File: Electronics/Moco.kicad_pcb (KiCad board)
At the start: 2 copper layers, 34 x 34 mm, 36 parts, among them J1 Conn_01x04, J2 Conn_01x01, J3 Conn_ARM_JTAG_SWD_10, J4 Conn_01x03, J5 Conn_01x01, J6 Conn_01x04, J8 Conn_01x01, J9 Conn_01x01, U1 EFM32PG22C200FxxIM32, U2 SP485EN, U3 TMAG5273, U4 DRV8311, Y1 ECS-384-CDX-1983

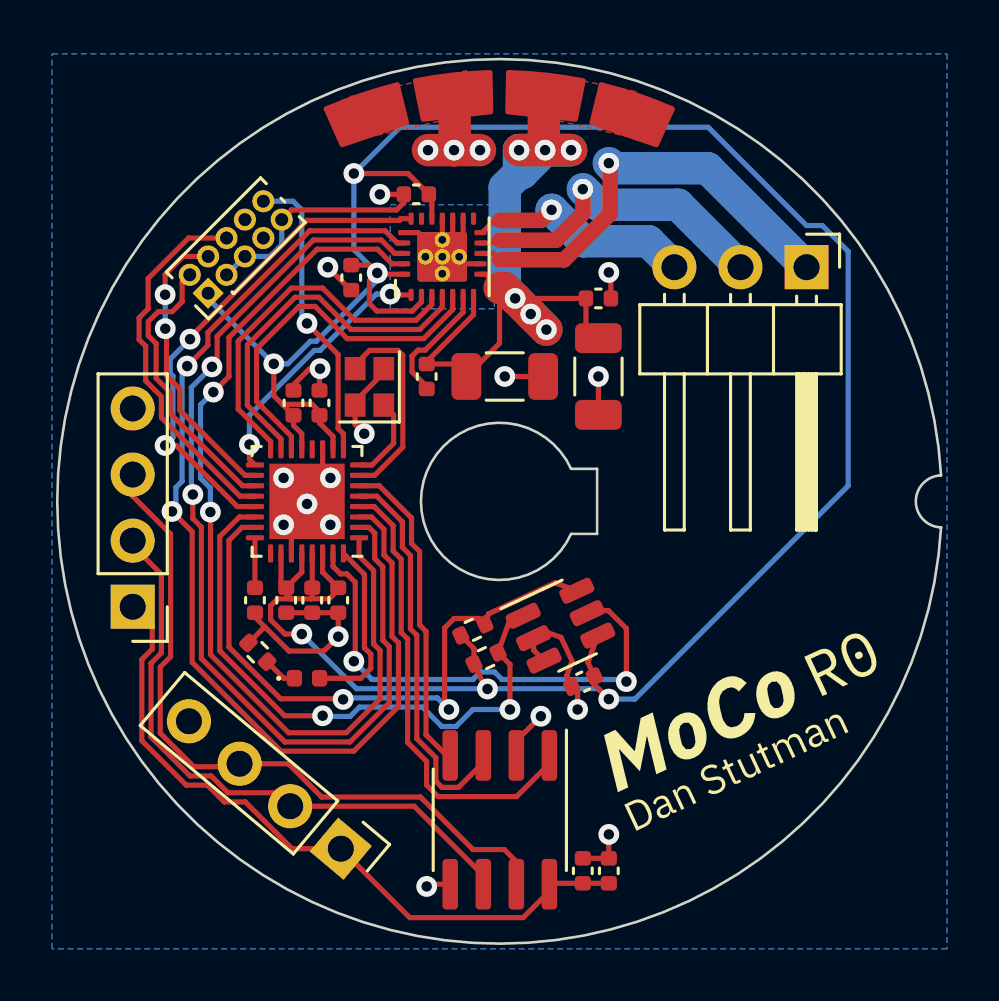
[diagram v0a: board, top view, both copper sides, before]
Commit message: Trade nFAULT for nSCS to avoid power on indeterminacy
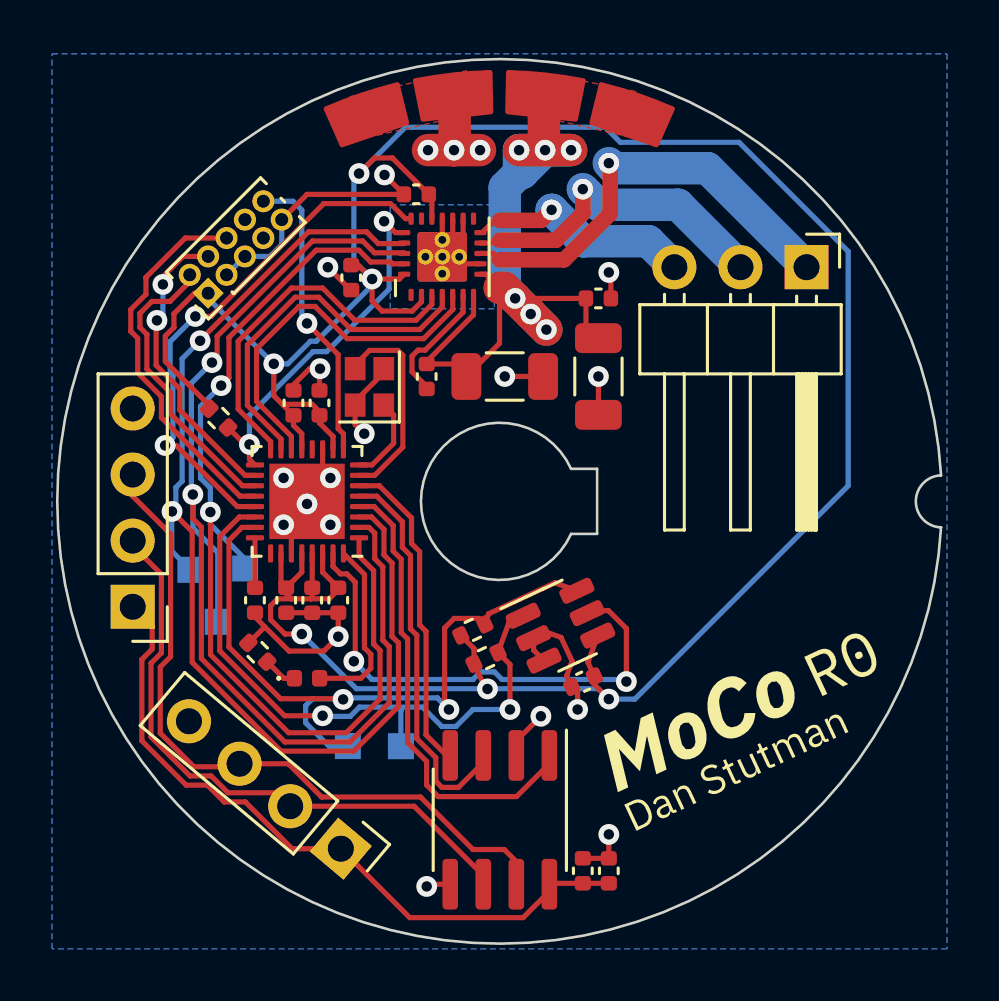
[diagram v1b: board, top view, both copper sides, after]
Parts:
- added R4: 10 kR, Resistor_SMD:R_0402_1005Metric, F.Cu at (39.2, 46.8)
- added TP1: TestPoint, TestPoint:TestPoint_Pad_1.0x1.0mm, B.Cu at (46.2, 59.4)
- added TP2: TestPoint, TestPoint:TestPoint_Pad_1.0x1.0mm, B.Cu at (40.2, 52.6)
- added TP3: TestPoint, TestPoint:TestPoint_Pad_1.0x1.0mm, B.Cu at (44.2, 59.4)
- added TP4: TestPoint, TestPoint:TestPoint_Pad_1.0x1.0mm, B.Cu at (39.2, 54.6)
- added TP5: TestPoint, TestPoint:TestPoint_Pad_1.0x1.0mm, B.Cu at (38.1, 52.6)
- added kibuzzard-624C45BD: G***, kibuzzard-624C45BD, B.Cu at (38.0, 51.2)
- added kibuzzard-624C45C7: G***, kibuzzard-624C45C7, B.Cu at (40.2, 51.2)
- added kibuzzard-624C45D0: G***, kibuzzard-624C45D0, B.Cu at (39.2, 56.0)
- added kibuzzard-624C45D8: G***, kibuzzard-624C45D8, B.Cu at (46.2, 60.8)
- added kibuzzard-624C45E2: G***, kibuzzard-624C45E2, B.Cu at (44.2, 60.8)
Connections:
- U1 pad 17: /~{FAULT} -> /DRV_~{SCS}
- U4 pad 1: /~{FAULT} -> unconnected-(U4-Pad1)
- U4 pad 20: GND -> /DRV_~{SCS}
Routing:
- net /DRV_~{SCS}: track 0.00 -> 14.1 mm, vias 0 -> 2
- net /~{FAULT}: track 10.2 -> 0.00 mm, vias 2 -> 0
- net +3V3: track 103.2 -> 108.9 mm
- net /SDI: track 38.5 -> 43.8 mm
- net /TMS_SCL: track 23.9 -> 28.2 mm
- net /SCLK: track 36.0 -> 38.7 mm
- net /SDO: track 41.2 -> 43.7 mm
- net GND: track 49.7 -> 47.7 mm
- net /TMS_SDA: track 23.2 -> 24.7 mm
- net /PWM_SYNC: track 19.5 -> 20.3 mm

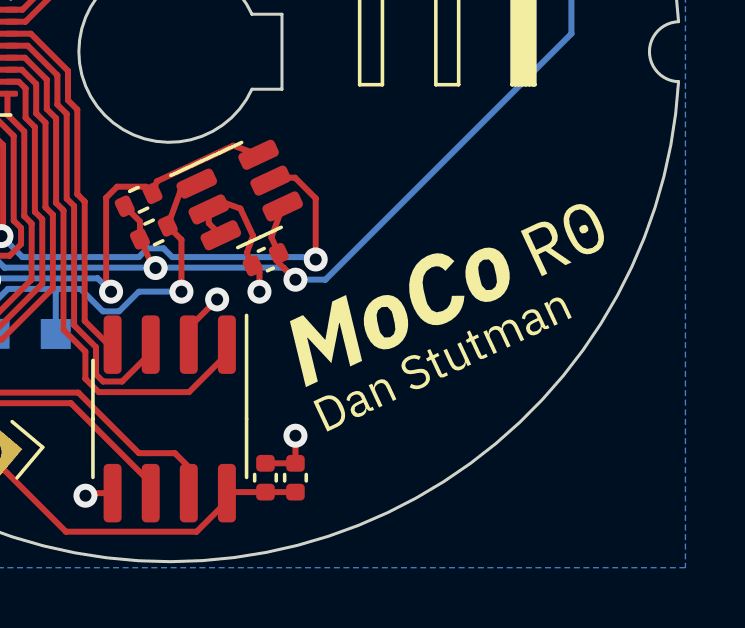
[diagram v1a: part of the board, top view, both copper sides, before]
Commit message: Update versioning scheme
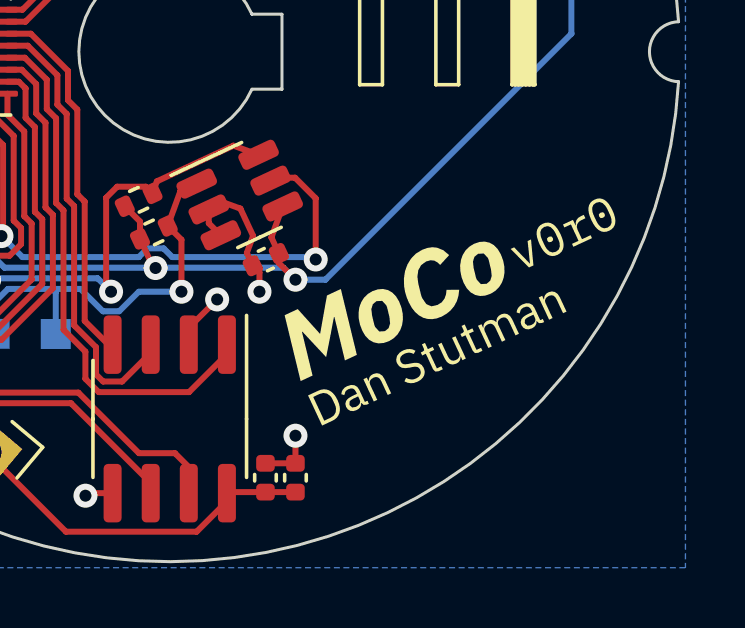
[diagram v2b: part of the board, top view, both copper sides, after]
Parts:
- removed kibuzzard-6246204B: G***, kibuzzard-6246204B
- added kibuzzard-624C491C: G***, kibuzzard-624C491C, F.Cu at (63.1, 56.0)
- moved kibuzzard-6244D452 0.27 mm to (58.9, 60.1)
- moved kibuzzard-6244CA09 0.27 mm to (57.5, 58.3)

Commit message: Update silk (I think)
I am not entirely sure what changes are in this commit. I think it is mostly
just silk modifications.
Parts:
- added kibuzzard-6257E5BB: G***, kibuzzard-6257E5BB, F.Cu at (38.2, 52.0)
- added kibuzzard-6257E5C8: G***, kibuzzard-6257E5C8, F.Cu at (44.0, 60.0)
- added kibuzzard-6257E666: G***, kibuzzard-6257E666, F.Cu at (34.0, 50.2)
- added kibuzzard-6257E666: G***, kibuzzard-6257E666, F.Cu at (39.8, 62.5)
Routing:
- net Vdrive: track 31.7 -> 32.7 mm
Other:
- outline, holes or cut-outs redrawn

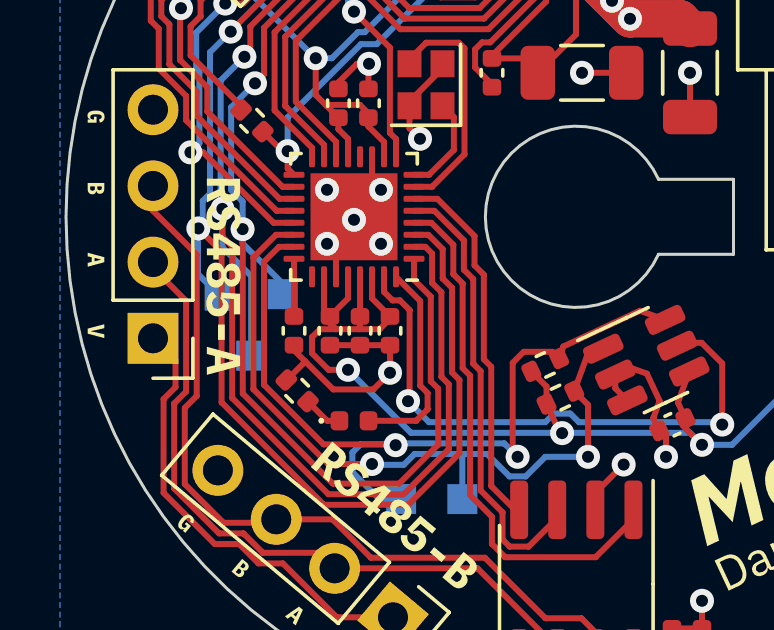
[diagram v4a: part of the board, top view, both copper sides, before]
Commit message: Update EFR32 part number
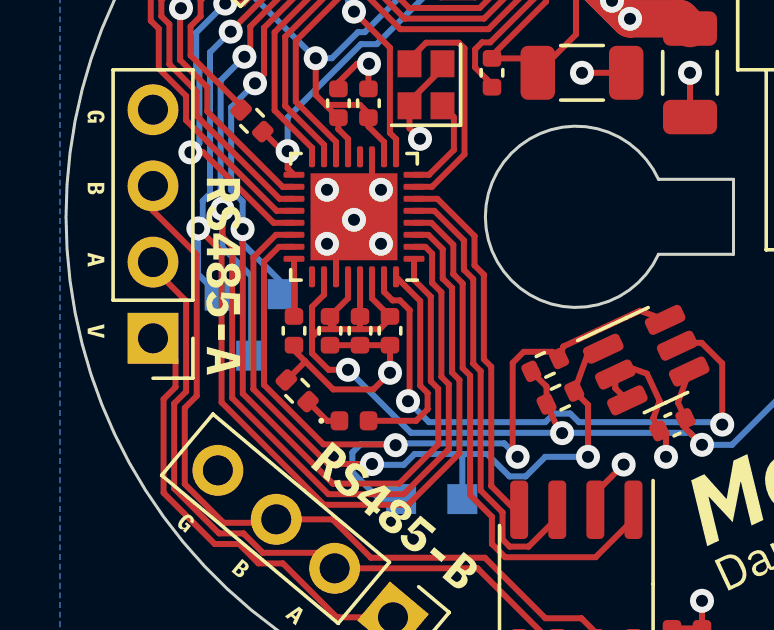
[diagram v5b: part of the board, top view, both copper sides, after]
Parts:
- C16: value 1 uF 6.3V X5R -> 0.1 uF 6.3V X5R
- C4: value 0.1 uF 6.3V X5R -> 1 uF 6.3V X5R
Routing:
- net +3V3: track 108.9 -> 110.3 mm
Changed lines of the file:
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@@
   (net 30 "/SWDIO")
   (net 31 "/SWCLK")
-  (net 32 "Net-(Y1-Pad3)")
-  (net 33 "Net-(Y1-Pad1)")
+  (net 32 "Net-(U1-Pad7)")
+  (net 33 "Net-(U1-Pad8)")
   (net 34 "unconnected-(J3-Pad7)")
   (net 35 "+5V")
@@
       (effects (font (size 1 1) (thickness 0.15)))
     )
-    (fp_text value "1 uF 6.3V X5R" (at 0 1.16 90) (layer "F.Fab") hide
+    (fp_text value "0.1 uF 6.3V X5R" (at 0 1.16 90) (layer "F.Fab") hide
       (effects (font (size 1 1) (thickness 0.15)))
     )
@@
       (net 5 "/UART_TX") (pinfunction "PC05") (pintype "bidirectional"))
     (pad "7" smd roundrect (at -2 1 180) (size 0.7 0.2) (layers "F.Cu" "F.Paste" "F.Mask") (roundrect_rratio 0.25)
-      (net 32 "Net-(Y1-Pad3)") (pinfunction "HFXTAL_I") (pintype "input"))
+      (net 32 "Net-(U1-Pad7)") (pinfunction "HFXTAL_I") (pintype "input"))
     (pad "8" smd roundrect (at -2 1.4 180) (size 0.7 0.2) (layers "F.Cu" "F.Paste" "F.Mask") (roundrect_rratio 0.25)
-      (net 33 "Net-(Y1-Pad1)") (pinfunction "HFXTAL_O") (pintype "output"))
+      (net 33 "Net-(U1-Pad8)") (pinfunction "HFXTAL_O") (pintype "output"))
     (pad "9" smd roundrect (at -1.4 2 180) (size 0.2 0.7) (layers "F.Cu" "F.Paste" "F.Mask") (roundrect_rratio 0.25)
       (net 10 "/~{RESET}") (pinfunction "~{RESET}") (pintype "input"))
@@
     (fp_line (start -1 0.3) (end -0.5 0.8) (layer "F.Fab") (width 0.1))
     (pad "1" smd rect (at -0.7 0.55 90) (size 0.9 0.8) (layers "F.Cu" "F.Paste" "F.Mask")
-      (net 33 "Net-(Y1-Pad1)") (pinfunction "1") (pintype "passive"))
+      (net 33 "Net-(U1-Pad8)") (pinfunction "1") (pintype "passive"))
     (pad "2" smd rect (at 0.7 0.55 90) (size 0.9 0.8) (layers "F.Cu" "F.Paste" "F.Mask")
       (net 2 "GND") (pinfunction "2") (pintype "passive"))
     (pad "3" smd rect (at 0.7 -0.55 90) (size 0.9 0.8) (layers "F.Cu" "F.Paste" "F.Mask")
-      (net 32 "Net-(Y1-Pad3)") (pinfunction "3") (pintype "passive"))
+      (net 32 "Net-(U1-Pad7)") (pinfunction "3") (pintype "passive"))
     (pad "4" smd rect (at -0.7 -0.55 90) (size 0.9 0.8) (layers "F.Cu" "F.Paste" "F.Mask")
       (net 2 "GND") (pinfunction "4") (pintype "passive"))
@@
       (effects (font (size 1 1) (thickness 0.15)))
     )
-    (fp_text value "0.1 uF 6.3V X5R" (at 0 1.16 90) (layer "F.Fab") hide
+    (fp_text value "1 uF 6.3V X5R" (at 0 1.16 90) (layer "F.Fab") hide
       (effects (font (size 1 1) (thickness 0.15)))
     )
@@
     (effects (font (size 0.5 0.5) (thickness 0.125)))
   )
-  (segment (start 41.6 52) (end 41.6 53.12) (width 0.2) (layer "F.Cu") (net 1))
   (segment (start 42 53.74648) (end 42.74648 53.74648) (width 0.2) (layer "F.Cu") (net 1))
   (segment (start 45.101554 42.301554) (end 45.485921 42.685921) (width 0.2) (layer "F.Cu") (net 1))
   (segment (start 41.8 53.32) (end 41.8 53.54648) (width 0.2) (layer "F.Cu") (net 1))
   (segment (start 38.275795 42) (end 38.8 42) (width 0.2) (layer "F.Cu") (net 1))
-  (segment (start 41.6 53.12) (end 41.8 53.32) (width 0.2) (layer "F.Cu") (net 1))
   (segment (start 42.4 52) (end 42.4 52.72) (width 0.2) (layer "F.Cu") (net 1))
   (segment (start 43.8 53.4) (end 43.45352 53.74648) (width 0.2) (layer "F.Cu") (net 1))
+  (segment (start 41.6 52) (end 41.6 52.6) (width 0.2) (layer "F.Cu") (net 1))
+  (segment (start 41.2 54.01348) (end 41.467 53.74648) (width 0.2) (layer "F.Cu") (net 1))
   (segment (start 45.485921 42.685921) (end 46.643321 42.685921) (width 0.2) (layer "F.Cu") (net 1))
   (segment (start 38.839376 46.308919) (end 37.15352 44.623063) (width 0.2) (layer "F.Cu") (net 1))
   (segment (start 47 42.329242) (end 47 42.065) (width 0.2) (layer "F.Cu") (net 1))
-  (segment (start 41.2 54.546521) (end 41.2 54.013479) (width 0.2) (layer "F.Cu") (net 1))
   (segment (start 45.101554 41.4535) (end 46.1515 41.4535) (width 0.2) (layer "F.Cu") (net 1))
   (segment (start 42.8 46.269192) (end 43.08 46.549192) (width 0.2) (layer "F.Cu") (net 1))
@@
   (segment (start 42.4 48) (end 42.4 47.4) (width 0.2) (layer "F.Cu") (net 1))
   (segment (start 49.017402 56.239137) (end 49.456925 57.181697) (width 0.2) (layer "F.Cu") (net 1))
-  (segment (start 41.2 54.013479) (end 41.466999 53.74648) (width 0.2) (layer "F.Cu") (net 1))
   (segment (start 42.4 47.4) (end 42.08 47.08) (width 0.2) (layer "F.Cu") (net 1))
   (segment (start 46.643321 42.685921) (end 47 42.329242) (width 0.2) (layer "F.Cu") (net 1))
   (segment (start 45.88 36.8) (end 47.28 38.2) (width 0.2) (layer "F.Cu") (net 1))
+  (segment (start 41.6 52.6) (end 41.2 53) (width 0.2) (layer "F.Cu") (net 1))
   (segment (start 37.15352 44.623063) (end 37.15352 43.648395) (width 0.2) (layer "F.Cu") (net 1))
   (segment (start 42.8 53.69296) (end 42.74648 53.74648) (width 0.2) (layer "F.Cu") (net 1))
   (segment (start 42.8 52) (end 42.8 53.32) (width 0.2) (layer "F.Cu") (net 1))
-  (segment (start 41.466999 53.74648) (end 42 53.74648) (width 0.2) (layer "F.Cu") (net 1))
+  (segment (start 41.2 54.546521) (end 41.2 54.01348) (width 0.2) (layer "F.Cu") (net 1))
   (segment (start 42.4 52.72) (end 41.8 53.32) (width 0.2) (layer "F.Cu") (net 1))
   (segment (start 54.2 57.6) (end 53.647854 57.047854) (width 0.2) (layer "F.Cu") (net 1))
   (segment (start 43.2 52.72) (end 43.8 53.32) (width 0.2) (layer "F.Cu") (net 1))
+  (segment (start 41.2 53) (end 41.2 54.546521) (width 0.2) (layer "F.Cu") (net 1))
   (segment (start 45.101554 41.4535) (end 45.101554 42.301554) (width 0.2) (layer "F.Cu") (net 1))
   (segment (start 45.101554 41.4535) (end 44.568054 40.92) (width 0.2) (layer "F.Cu") (net 1))
@@
   (segment (start 37.15352 43.648395) (end 37.485952 43.315963) (width 0.2) (layer "F.Cu") (net 1))
   (segment (start 43.6 47.506974) (end 43.08 46.986974) (width 0.2) (layer "F.Cu") (net 1))
+  (segment (start 41.467 53.74648) (end 42 53.74648) (width 0.2) (layer "F.Cu") (net 1))
   (via (at 44.6 37.4) (size 0.8) (drill 0.4) (layers "F.Cu" "B.Cu") (net 1))
   (via (at 42.4 55.100011) (size 0.8) (drill 0.4) (layers "F.Cu" "B.Cu") (net 1))
@@
   (group "" (id 093e0f3c-a4b3-4709-98e0-957c66f7e9e6)
     (members
-      03015993-67fa-4265-87b3-b7c734d16a0b
       0d3ee6ec-df59-456d-90a9-116ce4aef184
       1382190d-a40b-40df-b429-059cb272fba8
-      1f171868-fac2-4e0d-9075-5f6cd6da7010
       24baab14-c1ed-4f83-868b-cbafc0523fee
       2b6dc378-9ac7-4bdd-b185-57e1888b7bfc

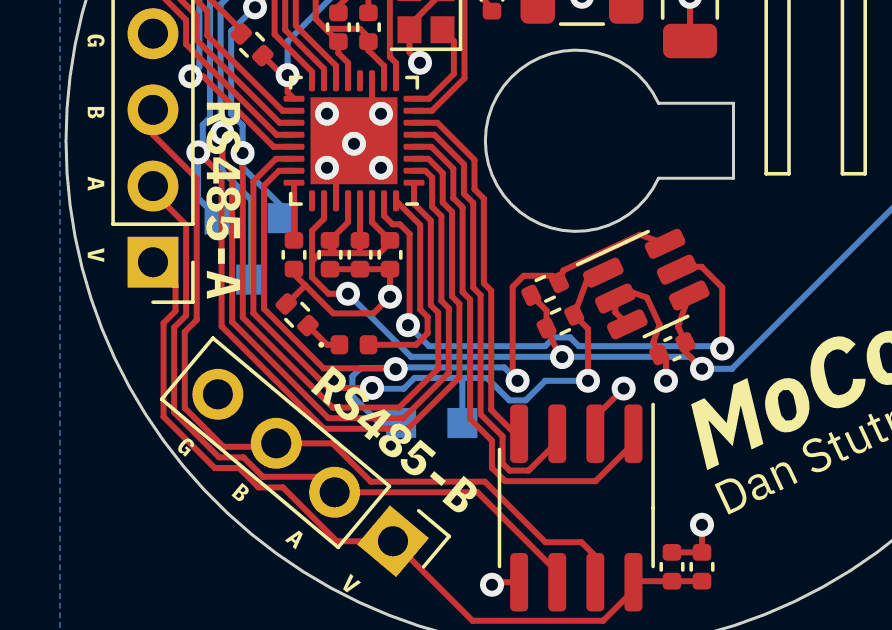
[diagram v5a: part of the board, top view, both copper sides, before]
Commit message: Improve decoupling
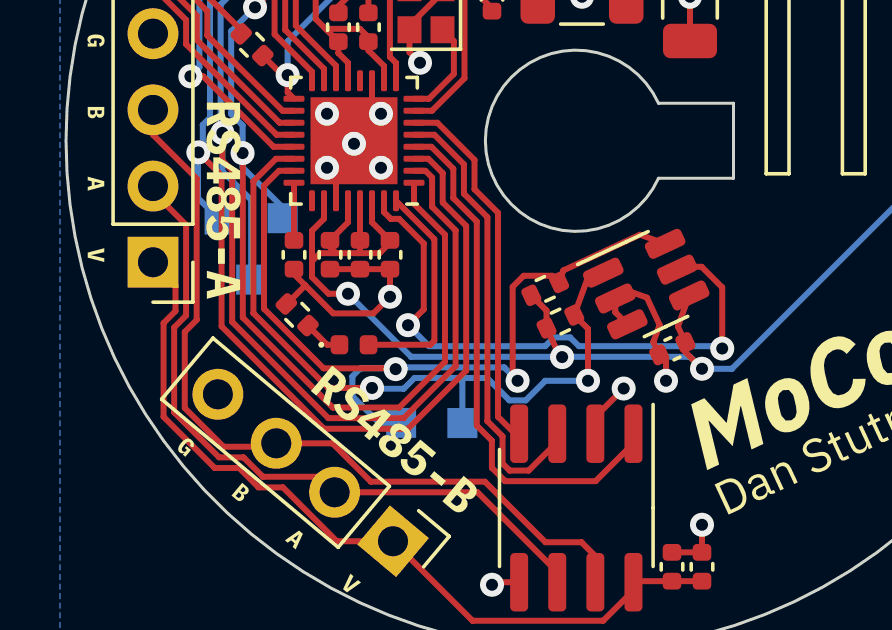
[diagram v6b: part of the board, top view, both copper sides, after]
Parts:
- C1: value VAL -> 1 uF 6.3V X5R
- C16: value 0.1 uF 6.3V X5R -> 0.1 + 2.7 uF 6.3V X5R
- C4: value 1 uF 6.3V X5R -> 0.1 + 1 uF 6.3V X5R
- C6: value 1 uF 6.3V X5R -> 0.01 + 1 uF 6.3V X5R
